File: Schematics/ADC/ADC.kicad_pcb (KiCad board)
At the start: 2 copper layers, 29.1 x 16.1 mm, 12 parts, among them J1 2-pin-header, J2 2-pin-header, J3 Conn_01x01, U1 ADS1115IDGST

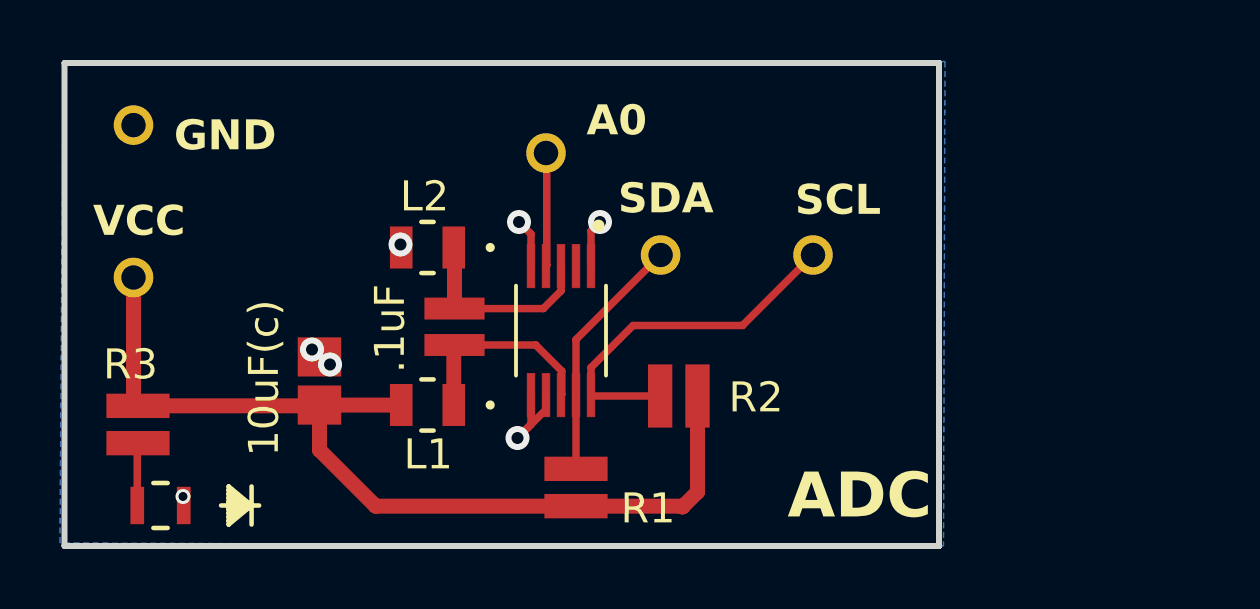
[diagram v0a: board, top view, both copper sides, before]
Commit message: updated schematic, layout and parts library
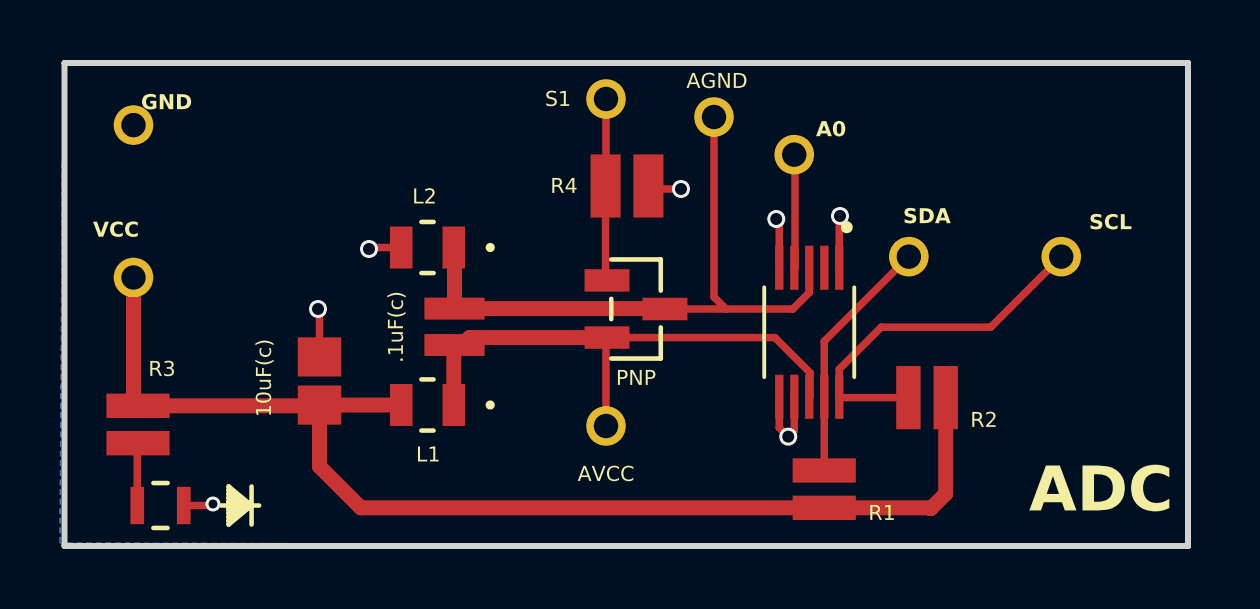
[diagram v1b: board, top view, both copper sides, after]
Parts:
- added AGND: Conn_01x01, pPSI:1 pin header, F.Cu at (40.9, 14.2)
- added AVCC: Conn_01x01, pPSI:1 pin header, F.Cu at (37.3, 24.5)
- added R4: 10k, pPSI:10kohm resistor, F.Cu at (38.0, 16.5)
- added S1: Conn_01x01, pPSI:1 pin header, F.Cu at (37.3, 13.6)
- added T1: PNP, pPSI:PNP Transistor, F.Cu at (38.3, 20.6)
- C2: value .1uF -> .1uF(c)
- moved J1 8.28 mm to (47.4, 18.9)
- moved J3 8.28 mm to (43.6, 15.5)
- moved R1 8.28 mm to (44.6, 26.6)
- moved U1 8.28 mm to (44.1, 21.4)
- moved R2 8.28 mm to (48.0, 23.6)
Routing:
- net /AGND: track 6.67 -> 21.5 mm
- net /AVCC: track 6.76 -> 18.2 mm
- net /VCC: track 31.4 -> 40.0 mm
- net /S1: track 0.00 -> 6.07 mm
- net /GND: track 6.67 -> 11.1 mm
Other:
- board size 29.1 x 16.1 mm -> 37.5 x 16.1 mm
